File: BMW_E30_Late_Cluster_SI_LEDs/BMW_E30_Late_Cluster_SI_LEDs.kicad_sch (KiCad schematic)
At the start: 0 parts

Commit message: Completed Schematic + Layout for SI LED
Additional labels were added to the SI board schematic to denote which pin controls which light on the LED board.
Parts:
- added D1: LED_G1, LED_THT:LED_D3.0mm, symbol Device:LED
- added D2: LED_G2, LED_THT:LED_D3.0mm, symbol Device:LED
- added D3: LED_G3, LED_THT:LED_D3.0mm, symbol Device:LED
- added D4: LED_G4, LED_THT:LED_D3.0mm, symbol Device:LED
- added D5: LED_G5, LED_THT:LED_D3.0mm, symbol Device:LED
- added D6: LED_Y, LED_THT:LED_D3.0mm, symbol Device:LED
- added D7: LED_R, LED_THT:LED_D3.0mm, symbol Device:LED
- added J1: SI Board Connector, Connector_PinSocket_2.54mm:PinSocket_1x12_P2.54mm_Horizontal, symbol Connector:Conn_01x12_Socket
- added LA1: Inspection Lamp, SI_THT:Lamp_D4.0mm_Horizontal_O3.81mm_Z2.0mm, symbol Device:Lamp
- added LA2: 12 Month Indicator Lamp, SI_THT:Lamp_D4.0mm_Horizontal_O3.81mm_Z2.0mm, symbol Device:Lamp
- added LA3: Oil Service Lamp, SI_THT:Lamp_D4.0mm_Horizontal_O3.81mm_Z2.0mm, symbol Device:Lamp
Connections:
- new net: D7.1 (K), J1.3 (Pin_3)
- new net: D1.2 (A), D2.2 (A), D3.2 (A), D4.2 (A), D5.2 (A), D6.2 (A), D7.2 (A), J1.2 (Pin_2)
- new net: J1.10 (Pin_10), LA2.1 (-)
- new net: D4.1 (K), J1.6 (Pin_6)
- new net: J1.11 (Pin_11), LA3.2 (+)
- new net: D1.1 (K), J1.12 (Pin_12)
- new net: D6.1 (K), J1.4 (Pin_4)
- new net: D5.1 (K), J1.5 (Pin_5)
- new net: D3.1 (K), J1.7 (Pin_7)
- new net: D2.1 (K), J1.8 (Pin_8)
- new net: J1.9 (Pin_9), LA1.1 (-)
- new net VCC_T15: J1.1 (Pin_1), LA1.2 (+), LA2.2 (+), LA3.1 (-)
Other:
- company: (none) -> Reagan Ansel
- title: (none) -> SI Indicator Lights

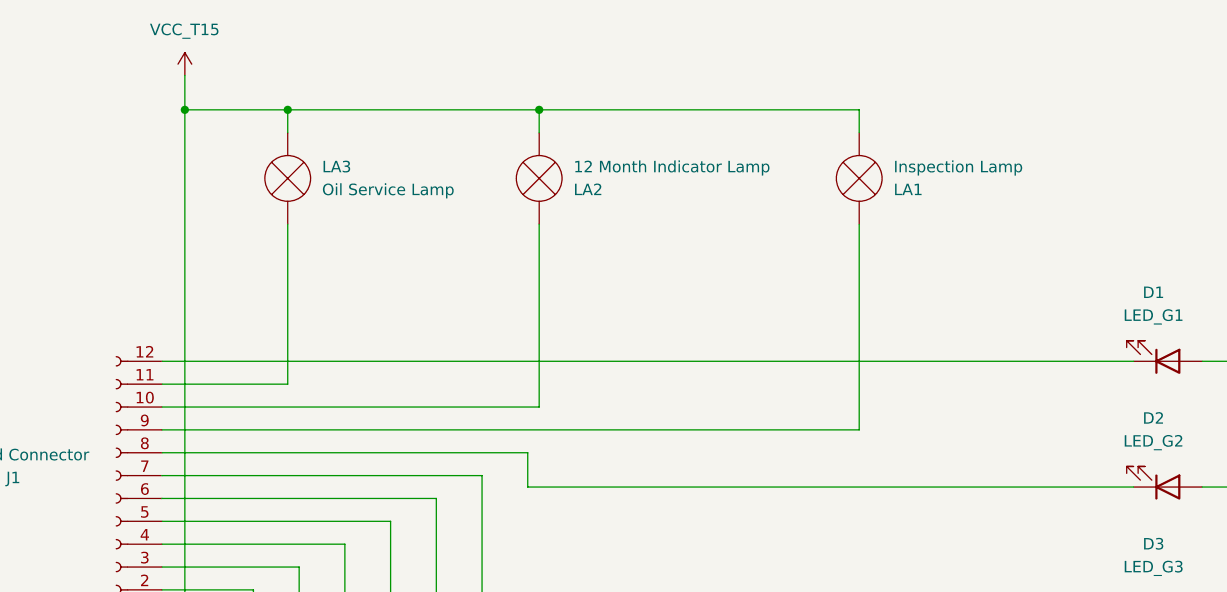
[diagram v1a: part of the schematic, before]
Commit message: Updates for GBR files
Slight stylistic improvements for GBR files as well as added some links to parts on digikey.
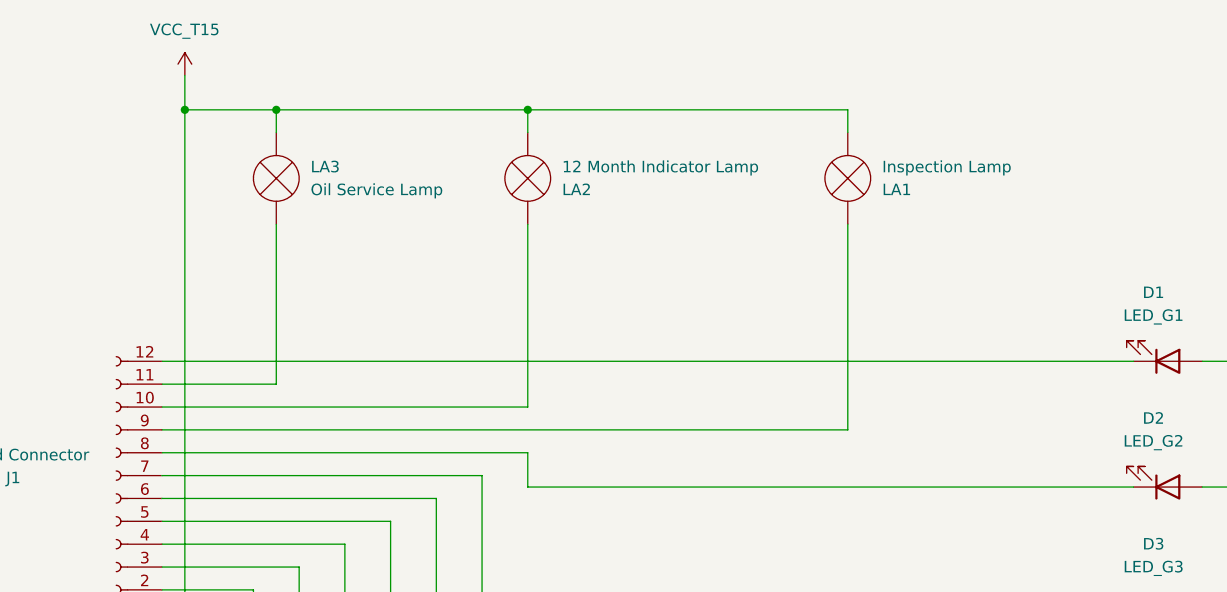
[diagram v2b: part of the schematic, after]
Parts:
- J1: Vendor Link (none) -> https://www.digikey.com/en/products/detail/sullins-connecto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
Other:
- moved on the sheet: LA1, LA2, LA3
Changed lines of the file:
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@@
 	)
 	(junction
-		(at 100.33 33.02)
-		(diameter 0)
-		(color 0 0 0 0)
-	)
-	(junction
-		(at 128.27 33.02)
+		(at 99.06 33.02)
 		(diameter 0)
 		(color 0 0 0 0)
@@
 		(color 0 0 0 0)
 	)
-	(wire
-		(pts
-			(xy 100.33 33.02) (xy 128.27 33.02)
+	(junction
+		(at 127 33.02)
+		(diameter 0)
+		(color 0 0 0 0)
+	)
+	(wire
+		(pts
+			(xy 99.06 33.02) (xy 88.9 33.02)
 		)
 		(stroke
@@
 	(wire
 		(pts
-			(xy 100.33 35.56) (xy 100.33 33.02)
+			(xy 99.06 35.56) (xy 99.06 33.02)
 		)
 		(stroke
@@
 	(wire
 		(pts
+			(xy 99.06 33.02) (xy 127 33.02)
+		)
+		(stroke
+			(width 0)
+			(type default)
+		)
+	)
+	(wire
+		(pts
 			(xy 201.93 130.81) (xy 207.01 130.81)
 		)
@@
 	(wire
 		(pts
-			(xy 163.83 45.72) (xy 163.83 68.58)
+			(xy 162.56 45.72) (xy 162.56 68.58)
 		)
 		(stroke
@@
 	(wire
 		(pts
-			(xy 163.83 33.02) (xy 163.83 35.56)
+			(xy 162.56 33.02) (xy 162.56 35.56)
 		)
 		(stroke
@@
 	(wire
 		(pts
-			(xy 128.27 45.72) (xy 128.27 66.04)
-		)
-		(stroke
-			(width 0)
-			(type default)
-		)
-	)
-	(wire
-		(pts
-			(xy 100.33 33.02) (xy 88.9 33.02)
+			(xy 127 45.72) (xy 127 66.04)
 		)
 		(stroke
@@
 	(wire
 		(pts
-			(xy 128.27 33.02) (xy 128.27 35.56)
+			(xy 127 33.02) (xy 127 35.56)
 		)
 		(stroke
@@
 	(wire
 		(pts
-			(xy 86.36 66.04) (xy 128.27 66.04)
+			(xy 86.36 66.04) (xy 127 66.04)
 		)
 		(stroke
@@
 	(wire
 		(pts
-			(xy 100.33 63.5) (xy 86.36 63.5)
-		)
-		(stroke
-			(width 0)
-			(type default)
-		)
-	)
-	(wire
-		(pts
-			(xy 163.83 68.58) (xy 86.36 68.58)
+			(xy 99.06 63.5) (xy 86.36 63.5)
+		)
+		(stroke
+			(width 0)
+			(type default)
+		)
+	)
+	(wire
+		(pts
+			(xy 162.56 68.58) (xy 86.36 68.58)
 		)
 		(stroke
@@
 	(wire
 		(pts
-			(xy 128.27 33.02) (xy 163.83 33.02)
-		)
-		(stroke
-			(width 0)
-			(type default)
-		)
-	)
-	(wire
-		(pts
-			(xy 100.33 45.72) (xy 100.33 63.5)
+			(xy 127 33.02) (xy 162.56 33.02)
+		)
+		(stroke
+			(width 0)
+			(type default)
+		)
+	)
+	(wire
+		(pts
+			(xy 99.06 45.72) (xy 99.06 63.5)
 		)
 		(stroke
@@
 			)
 		)
+		(property "Vendor Link" ""
+			(at 198.12 144.78 0)
+			(effects
+				(font
+					(size 1.27 1.27)
+				)
+				(hide yes)
+			)
+		)
 		(pin "2"
 		)
@@
 	(symbol
 		(lib_id "Device:Lamp")
-		(at 128.27 40.64 0)
+		(at 127 40.64 0)
 		(mirror y)
 		(unit 1)
@@
 		(dnp no)
 		(property "Reference" "LA2"
-			(at 132.08 41.9101 0)
+			(at 130.81 41.9101 0)
 			(effects
 				(font
@@
 		)
 		(property "Value" "12 Month Indicator Lamp"
-			(at 132.08 39.3701 0)
+			(at 130.81 39.3701 0)
 			(effects
 				(font
@@
 		)
 		(property "Footprint" "SI_THT:Lamp_D4.0mm_Horizontal_O3.81mm_Z2.0mm"
-			(at 128.27 38.1 90)
+			(at 127 38.1 90)
 			(effects
 				(font
@@
 		)
 		(property "Datasheet" "~"
-			(at 128.27 38.1 90)
+			(at 127 38.1 90)
 			(effects
 				(font
@@
 		)
 		(property "Description" "Lamp"
-			(at 128.27 40.64 0)
+			(at 127 40.64 0)
+			(effects
+				(font
+					(size 1.27 1.27)
+				)
+				(hide yes)
+			)
+		)
+		(property "Vendor Link" ""
+			(at 127 40.64 0)
 			(effects
 				(font
@@
 			)
 		)
+		(property "Vendor Link" ""
+			(at 198.12 102.87 0)
+			(effects
+				(font
+					(size 1.27 1.27)
+				)
+				(hide yes)
+			)
+		)
 		(pin "2"
 		)
@@
 			)
 		)
-		(property "Datasheet" "~"
+		(property "Datasheet" "https://mm.digikey.com/Volume0/opasdata/d220001/medias/docus/937/Female_Headers.100_DS.pdf"
 			(at 81.28 76.2 0)
 			(effects
@@
 		)
 		(property "Description" "Generic connector, single row, 01x12, script generated"
+			(at 81.28 76.2 0)
+			(effects
+				(font
+					(size 1.27 1.27)
+				)
+				(hide yes)
+			)
+		)
+		(property "Vendor Link" "https://www.digikey.com/en/products/detail/sullins-connector-solutions/PPTC121LGBN-RC/775906"
 			(at 81.28 76.2 0)
 			(effects
@@
 			)
 		)
+		(property "Vendor Link" ""
+			(at 198.12 88.9 0)
+			(effects
+				(font
+					(size 1.27 1.27)
+				)
+				(hide yes)
+			)
+		)
 		(pin "2"
 		)
@@
 			)
 		)
+		(property "Vendor Link" ""
+			(at 198.12 60.96 0)
+			(effects
+				(font
+					(size 1.27 1.27)
+				)
+				(hide yes)
+			)
+		)
 		(pin "2"
 		)
@@
 	(symbol
 		(lib_id "Device:Lamp")
-		(at 163.83 40.64 0)
+		(at 162.56 40.64 0)
 		(mirror y)
 		(unit 1)
@@
 		(dnp no)
 		(property "Reference" "LA1"
-			(at 167.64 41.9101 0)
+			(at 166.37 41.9101 0)
 			(effects
 				(font
@@
 		)
 		(property "Value" "Inspection Lamp"
-			(at 167.64 39.3701 0)
+			(at 166.37 39.3701 0)
 			(effects
 				(font
@@
 		)
 		(property "Footprint" "SI_THT:Lamp_D4.0mm_Horizontal_O3.81mm_Z2.0mm"
-			(at 163.83 38.1 90)
+			(at 162.56 38.1 90)
 			(effects
 				(font
@@
 		)
 		(property "Datasheet" "~"
-			(at 163.83 38.1 90)
+			(at 162.56 38.1 90)
 			(effects
 				(font
@@
 		)
 		(property "Description" "Lamp"
-			(at 163.83 40.64 0)
+			(at 162.56 40.64 0)
+			(effects
+				(font
+					(size 1.27 1.27)
+				)
+				(hide yes)
+			)
+		)
+		(property "Vendor Link" ""
+			(at 162.56 40.64 0)
 			(effects
 				(font
@@
 			)
 		)
+		(property "Vendor Link" ""
+			(at 198.12 116.84 0)
+			(effects
+				(font
+					(size 1.27 1.27)
+				)
+				(hide yes)
+			)
+		)
 		(pin "2"
 		)
@@
 			)
 		)
+		(property "Vendor Link" ""
+			(at 198.12 74.93 0)
+			(effects
+				(font
+					(size 1.27 1.27)
+				)
+				(hide yes)
+			)
+		)
 		(pin "2"
 		)
@@
 			)
 		)
+		(property "Vendor Link" ""
+			(at 198.12 130.81 0)
+			(effects
+				(font
+					(size 1.27 1.27)
+				)
+				(hide yes)
+			)
+		)
 		(pin "2"
 		)
@@
 	(symbol
 		(lib_id "Device:Lamp")
-		(at 100.33 40.64 180)
+		(at 99.06 40.64 180)
 		(unit 1)
 		(exclude_from_sim no)
@@
 		(fields_autoplaced yes)
 		(property "Reference" "LA3"
-			(at 104.14 39.3699 0)
+			(at 102.87 39.3699 0)
 			(effects
 				(font
@@
 		)
 		(property "Value" "Oil Service Lamp"
-			(at 104.14 41.9099 0)
+			(at 102.87 41.9099 0)
 			(effects
 				(font
@@
 		)
 		(property "Footprint" "SI_THT:Lamp_D4.0mm_Horizontal_O3.81mm_Z2.0mm"
-			(at 100.33 43.18 90)
+			(at 99.06 43.18 90)
 			(effects
 				(font
@@
 		)
 		(property "Datasheet" "~"
-			(at 100.33 43.18 90)
+			(at 99.06 43.18 90)
 			(effects
 				(font
@@
 		)
 		(property "Description" "Lamp"
-			(at 100.33 40.64 0)
-			(effects
-				(font
+			(at 99.06 40.64 0)
+			(effects
+				(font
+					(size 1.27 1.27)
+				)
+				(hide yes)
+			)
+		)
+		(property "Vendor Link" ""
+			(at 99.06 40.64 0)
+			(effects
+				(font

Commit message: Update Schematic PDFs
Added updates to schematic pdf documents for consistency
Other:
- company: Reagan Ansel -> Reans
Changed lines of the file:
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@@
 	(title_block
 		(title "SI Indicator Lights")
+		(date "2026-06-03")
 		(rev "0")
-		(company "Reagan Ansel")
+		(company "Reans")
+		(comment 1 "Reagan Ansel")
 	)
 	(junction
@@
 		)
 		(instances
-			(project ""
+			(project "BMW_E30_Late_Cluster_SI_LEDs"
 				(path "/764d84c7-63fb-41bb-b1c4-5da1c53525b0"
 					(reference "J1")
@@
 	)
 	(embedded_fonts no)
+	(embedded_files
+		(file
+			(name "reans_sheet_template.kicad_wks")
+			(type worksheet)
+			(data |KLUv/WD/Cu0XAPbhaSEA1TZqxSYVNDoEMnCBWkUAFLHYT8LfLc64wmSW/n9CwQRfAFoAZABfTlM7
+				Cd4PPZP4H186+DUZmyftazMZJC2P8bFwUWq25kUL8mvHwkXR9pEtP+RPAAACHc97OanDZJkyfiu6
+				ZexMnfGD2a9nCIBAQaOUVnXWvtiW2T8EQKDkgCwiGFoOIdn/etgijP3Ss7lq001Ur56Xy2XSChD4
+				izG0r9ol7kx06g/5X/6a1VV7XqJQDq990Dues9+Mwx979pw4IR4v7ePbb9d8i9eDM9hT/3WSxGHt
+				2uJ1q+pJaX8GA4vQjuDbzqhJOcfXfePbr1LR9rtrPIGhJBC7qR8kM8Z09g4omXCSTTKynjjiS1u1
+				q3CTj080beoGpaw+TAqJdN6Eq1gUW6JrkAYXdfWk9EBhnWkl7tsUFo7ieR1p0Ah/UJFzFgWBwsys
+				itUDRWfNENlvxpauoBUjcUhlrs3u12aulxf0XKs+aBalZRWr16FaFa1zTkqrrWV11qovCsPoB+Ee
+				j0iCNBBdsEPihDapC6udeZCNyxjfJvk4juFpWkVZjw3CObqFDYCaoBFNhdgMSQqSFDLMAYBEhObI
+				NmZkXfEEgg31YlRO4GceOtZZSD4tPZJ8rJ74G8PkjH1JKkKawsKGheoJuP2+IlY18ntrNC2s74Pr
+				DVe+cSgd0L7HteZMeDaXmooSSh/c+bVoVTYLk6RKN7Cv2UoaCAZv6YCSS6nbIQTWD7UwQeis5W/V
+				g0dYgB5CyE6HNFbmmlkm5KySJ6yIRrRM5Uc4pc8u9BJFUDGI5kCOG6xadygVBOu2LFloyz3FUwK0
+				K2QvICvncQgSH7pSFluywCLJ0Rwlm2f0GkYN7sFxT4mPYCI2kaL4bSAlPOhlas5v4CmJJDLxSXKn
+				Odp9OHfwRZI7o8xhC2+Z4AAEWT5Rojog0dbMToQXcXHPsDoOuhAAXPmNnp2jRa7V/EUBa9S+lvzC
+				Ux9y2yG0bmId6AOKOjzjaHSplt4lCml0x3i3uxaxGR+0Cg==|
+			)
+			(checksum "582015C87F5C50DCCFBFE692861C814F")
+		)
+	)
 )
